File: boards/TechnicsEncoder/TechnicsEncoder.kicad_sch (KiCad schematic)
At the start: 33 parts, among them J1 ISP, J2 Bender, J3 Technics, J4 SelectRX, J5 MIDI In, J6 MIDI Out, J7 BoardCon, J8 PistonEncoder, U1 ATmega48-20P, U2 6N137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

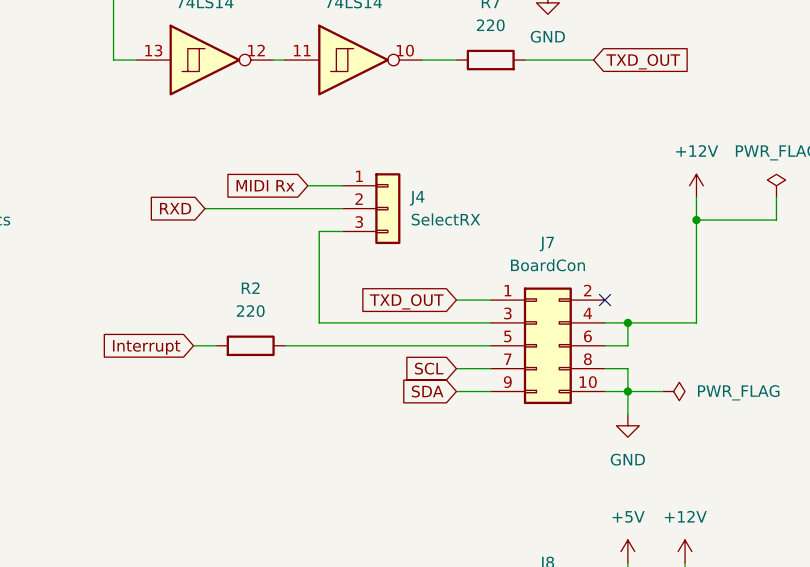
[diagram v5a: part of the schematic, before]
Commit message: Finished IO-Board PCB, switched RX/TX of board connectors for better routing
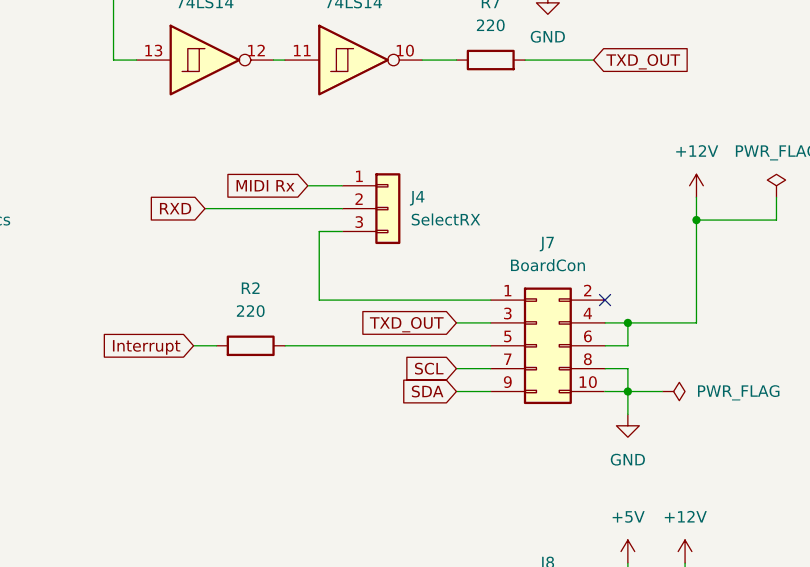
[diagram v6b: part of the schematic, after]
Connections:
- net TXD_OUT: now also J7.3 (Pin_3); no longer J7.1 (Pin_1)
- net at J4.3 (Pin_3): now also J7.1 (Pin_1); no longer J7.3 (Pin_3)
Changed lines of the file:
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@@
-	(wire
-		(pts
-			(xy 199.39 109.22) (xy 199.39 99.06)
-		)
-		(stroke
-			(width 0)
-			(type default)
-		)
-	)
 	(wire
 		(pts
@@
 	(wire
 		(pts
-			(xy 199.39 109.22) (xy 218.44 109.22)
-		)
-		(stroke
-			(width 0)
-			(type default)
-		)
-	)
-	(wire
-		(pts
 			(xy 39.37 74.93) (xy 57.15 74.93)
 		)
@@
 	(wire
 		(pts
+			(xy 199.39 106.68) (xy 199.39 99.06)
+		)
+		(stroke
+			(width 0)
+			(type default)
+		)
+	)
+	(wire
+		(pts
 			(xy 130.81 76.2) (xy 137.16 76.2)
 		)
@@
 	(wire
 		(pts
+			(xy 214.63 109.22) (xy 218.44 109.22)
+		)
+		(stroke
+			(width 0)
+			(type default)
+		)
+	)
+	(wire
+		(pts
 			(xy 116.84 33.02) (xy 119.38 33.02)
 		)
@@
 	(wire
 		(pts
-			(xy 214.63 106.68) (xy 218.44 106.68)
+			(xy 199.39 106.68) (xy 218.44 106.68)
 		)
 		(stroke
@@
 	(global_label "TXD_OUT"
 		(shape input)
-		(at 214.63 106.68 180)
+		(at 214.63 109.22 180)
 		(fields_autoplaced yes)
 		(effects
@@
 		)
 		(property "Intersheetrefs" "${INTERSHEET_REFS}"
-			(at 203.6015 106.68 0)
-			(effects
-				(font
+			(at 203.6015 109.22 0)
+			(effects
+				(font

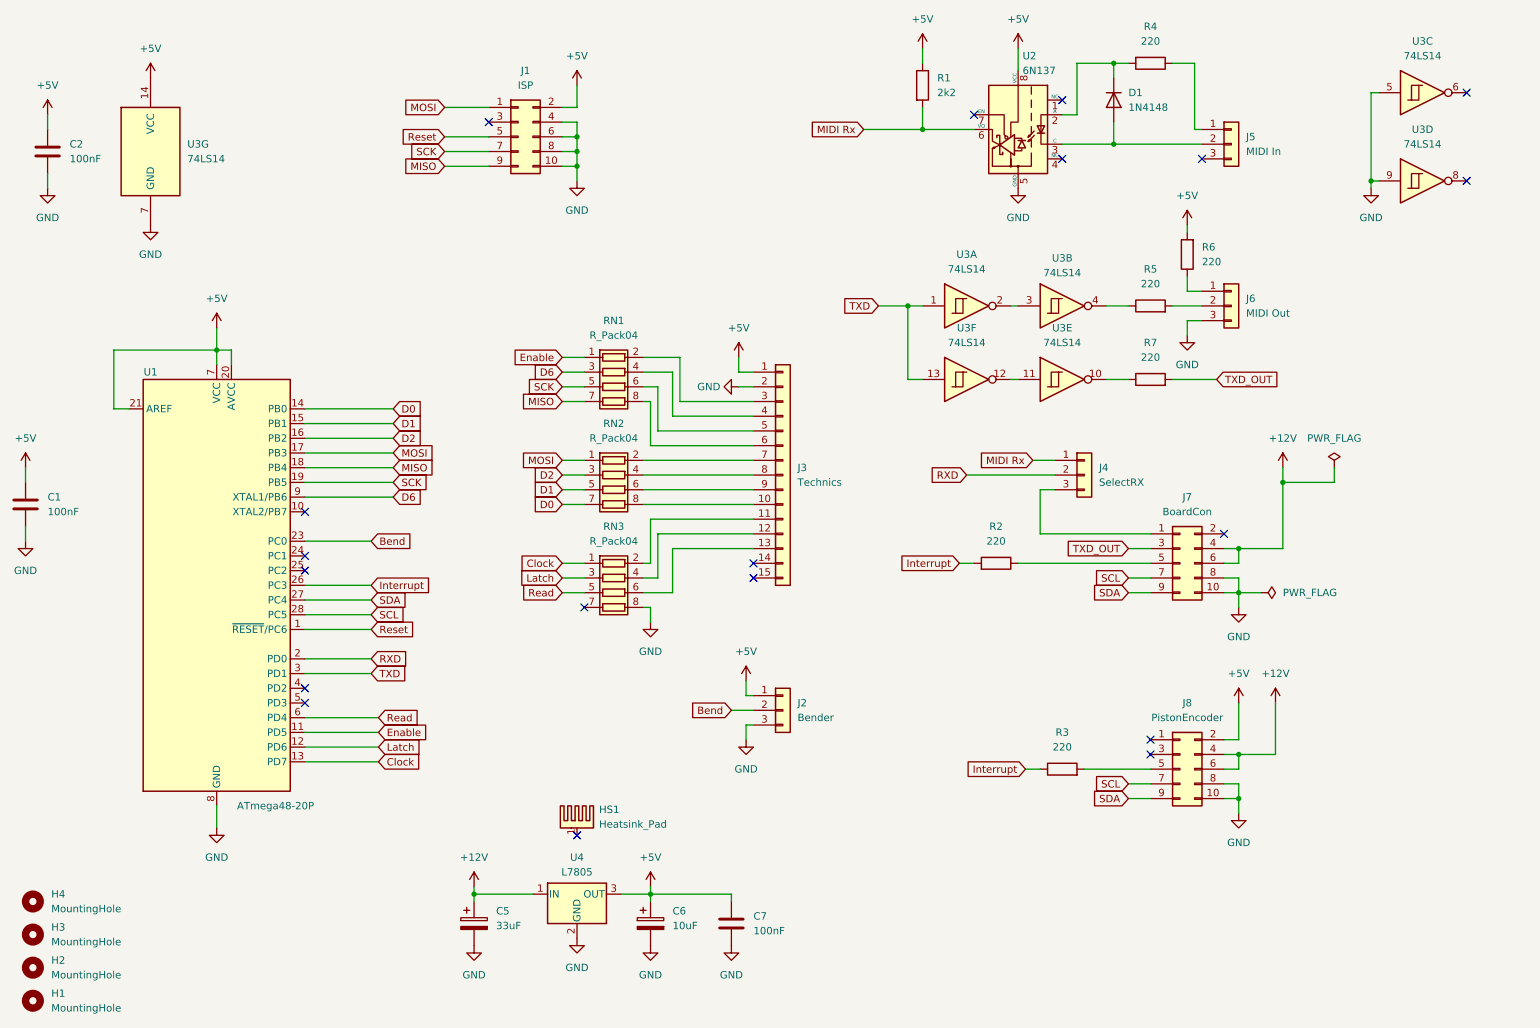
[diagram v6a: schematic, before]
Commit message: Fixed interrupt line to use open collector, added pullups to I2C lines
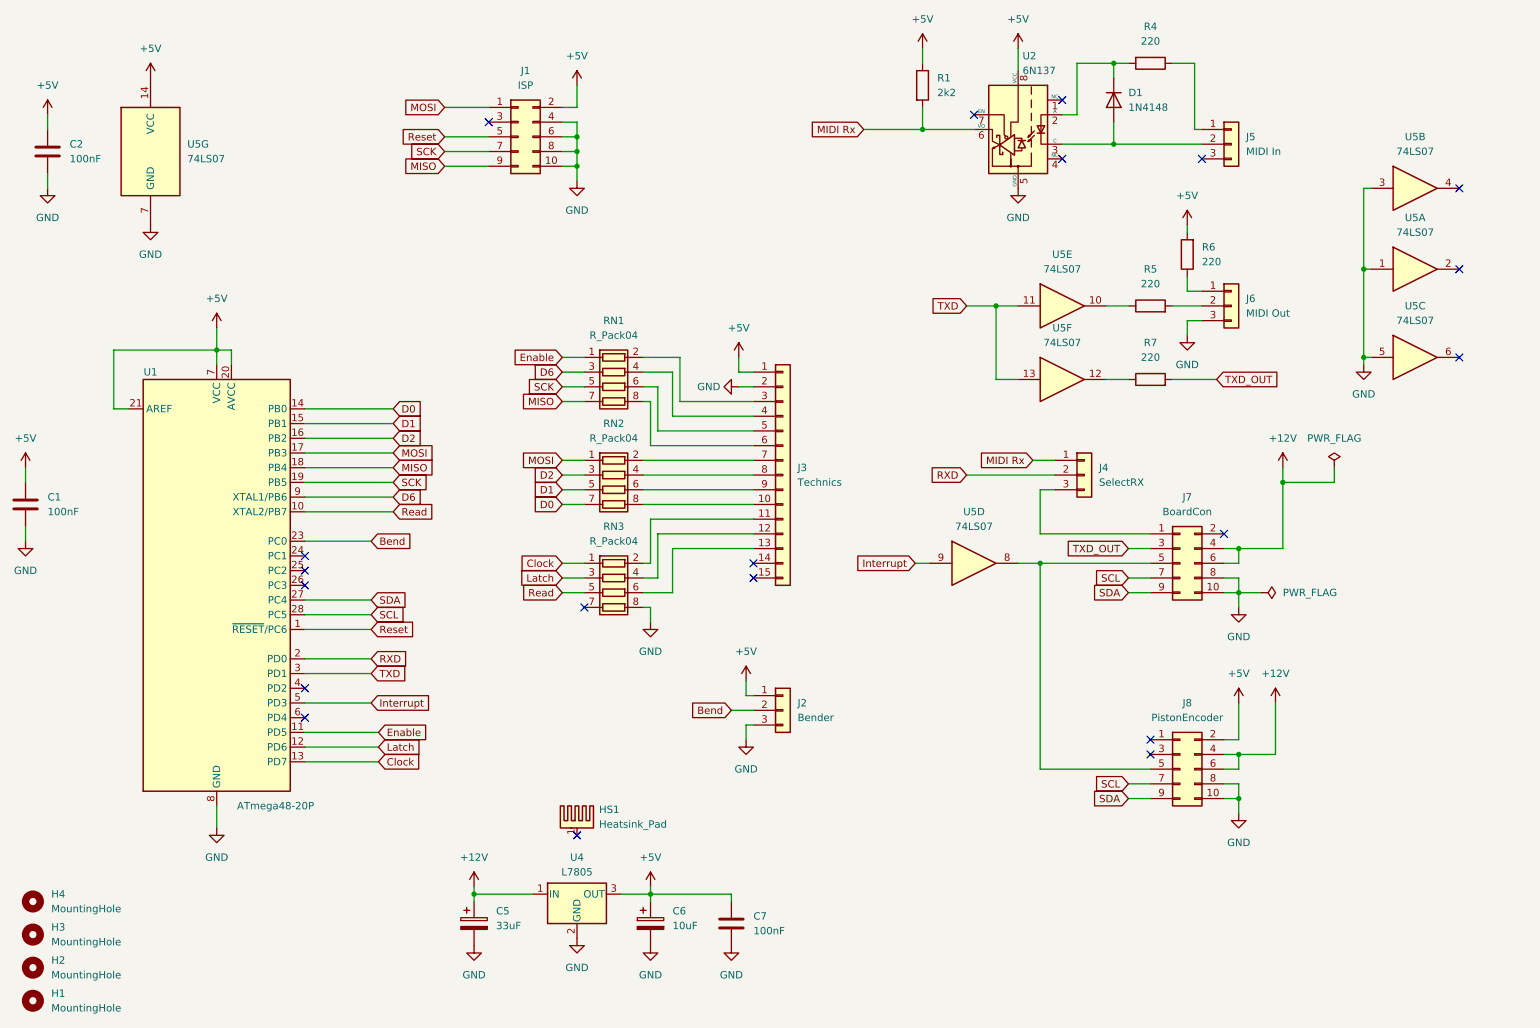
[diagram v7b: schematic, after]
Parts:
- removed R2, R3: 220, Resistor_THT:R_Axial_DIN0204_L3.6mm_D1.6mm_P7.62mm_Horizontal, symbol Device:R
- removed U3: 74LS14, Package_DIP:DIP-14_W7.62mm, symbol 74xx:74LS14
- added U5: 74LS07, Package_DIP:DIP-14_W7.62mm, symbol 74xx:74LS07
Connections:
- net +5V: now also U5.14 (VCC)
- net GND: now also U5.1, U5.3, U5.5, U5.7 (GND)
- net Interrupt: now also U1.5 (PD3), U5.9; no longer U1.26 (PC3)
- net Read: now also U1.10 (XTAL2/PB7); no longer U1.6 (PD4)
- net TXD: now also U5.11, U5.13
- net at R5.1: now also U5.10
- net at R7.1: now also U5.12
- net at J7.5 (Pin_5): now also J8.5 (Pin_5), U5.8
- no-connect marks 19 -> 20

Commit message: Added bypass caps to power supplies, use cheaper MAX232 IC.
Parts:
- added C3: 330nF, Capacitor_THT:C_Disc_D4.3mm_W1.9mm_P5.00mm, symbol Device:C
- RN1, RN2, RN3: value R_Pack04 -> 220
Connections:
- net +12V: now also C3.1
- net GND: now also C3.2
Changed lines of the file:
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@@
 	(wire
 		(pts
+			(xy 86.36 168.91) (xy 101.6 168.91)
+		)
+		(stroke
+			(width 0)
+			(type default)
+		)
+	)
+	(wire
+		(pts
 			(xy 72.39 118.11) (xy 83.82 118.11)
 		)
@@
 	(wire
 		(pts
+			(xy 86.36 170.18) (xy 86.36 168.91)
+		)
+		(stroke
+			(width 0)
+			(type default)
+		)
+	)
+	(wire
+		(pts
 			(xy 231.14 147.32) (xy 233.68 147.32)
 		)
@@
 	)
 	(symbol
+		(lib_id "Device:C")
+		(at 86.36 173.99 0)
+		(unit 1)
+		(exclude_from_sim no)
+		(in_bom yes)
+		(on_board yes)
+		(dnp no)
+		(fields_autoplaced yes)
+		(property "Reference" "C3"
+			(at 90.17 172.7199 0)
+			(effects
+				(font
+					(size 1.27 1.27)
+				)
+				(justify left)
+			)
+		)
+		(property "Value" "330nF"
+			(at 90.17 175.2599 0)
+			(effects
+				(font
+					(size 1.27 1.27)
+				)
+				(justify left)
+			)
+		)
+		(property "Footprint" "Capacitor_THT:C_Disc_D4.3mm_W1.9mm_P5.00mm"
+			(at 87.3252 177.8 0)
+			(effects
+				(font
+					(size 1.27 1.27)
+				)
+				(hide yes)
+			)
+		)
+		(property "Datasheet" "~"
+			(at 86.36 173.99 0)
+			(effects
+				(font
+					(size 1.27 1.27)
+				)
+				(hide yes)
+			)
+		)
+		(property "Description" "Unpolarized capacitor"
+			(at 86.36 173.99 0)
+			(effects
+				(font
+					(size 1.27 1.27)
+				)
+				(hide yes)
+			)
+		)
+		(pin "1"
+		)
+		(pin "2"
+		)
+		(instances
+			(project "TechnicsEncoder"
+				(path "/bada7ee2-3b4f-486d-8871-f40e51bae2c2"
+					(reference "C3")
+					(unit 1)
+				)
+			)
+		)
+	)
+	(symbol
 		(lib_id "Custom_Symbols:R_Pack04_SIL")
 		(at 125.73 116.84 270)
@@
 			)
 		)
-		(property "Value" "R_Pack04"
+		(property "Value" "220"
 			(at 125.73 107.95 90)
 			(effects
@@
 			)
 		)
-		(property "Value" "R_Pack04"
+		(property "Value" "220"
 			(at 125.73 72.39 90)
 			(effects
@@
 			)
 		)
-		(property "Value" "R_Pack04"
+		(property "Value" "220"
 			(at 125.73 90.17 90)
 			(effects
@@
 				)
 			)
+		)
+	)
+	(symbol
+		(lib_id "power:GND")
+		(at 86.36 177.8 0)
+		(unit 1)
+		(exclude_from_sim no)
+		(in_bom yes)
+		(on_board yes)
+		(dnp no)
+		(fields_autoplaced yes)
+		(property "Reference" "#PWR015"
+			(at 86.36 184.15 0)
+			(effects
+				(font
+					(size 1.27 1.27)
+				)
+				(hide yes)
+			)
+		)
+		(property "Value" "GND"
+			(at 86.36 182.88 0)
+			(effects
+				(font
+					(size 1.27 1.27)
+				)
+			)
+		)
+		(property "Footprint" ""
+			(at 86.36 177.8 0)
+			(effects
+				(font
+					(size 1.27 1.27)
+				)
+				(hide yes)
+			)
+		)
+		(property "Datasheet" ""
+			(at 86.36 177.8 0)
+			(effects
+				(font
+					(size 1.27 1.27)
+				)
+				(hide yes)
+			)
+		)
+		(property "Description" "Power symbol creates a global label with name \"GND\" , ground"
+			(at 86.36 177.8 0)
+			(effects
+				(font
+					(size 1.27 1.27)
+				)
+				(hide yes)
+			)
+		)
+		(pin "1"
+		)
+		(instances
+			(project "TechnicsEncoder"
+				(path "/bada7ee2-3b4f-486d-8871-f40e51bae2c2"
+					(reference "#PWR015")
+					(unit 1)
+				)
+			)
